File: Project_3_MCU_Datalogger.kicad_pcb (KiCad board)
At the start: 2 copper layers, 0 parts

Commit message: setup feuille PCB et importation 3D models
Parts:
- added BT1: Battery, Connector_PinHeader_2.54mm:PinHeader_1x02_P2.54mm_Vertical, F.Cu at (126.4, 94.8)
- added C1: 0.1u, Capacitor_SMD:C_0805_2012Metric, F.Cu at (148.8, 84.9)
- added C2: 0.1u, Capacitor_SMD:C_0805_2012Metric, F.Cu at (148.8, 87.9)
- added C3: 22p, Capacitor_SMD:C_0805_2012Metric, F.Cu at (148.8, 91.0)
- added C4: 22p, Capacitor_SMD:C_0805_2012Metric, F.Cu at (148.8, 94.0)
- added C5: 100n, Capacitor_SMD:C_0805_2012Metric, F.Cu at (148.8, 97.0)
- added D1: LED, LED_SMD:LED_0805_2012Metric, F.Cu at (153.2, 85.0)
- added D2: LED, LED_SMD:LED_0805_2012Metric, F.Cu at (153.2, 88.0)
- added H1: MountingHole, MountingHole:MountingHole_2.1mm, F.Cu at (127.0, 72.4)
- added H2: MountingHole, MountingHole:MountingHole_2.1mm, F.Cu at (127.0, 78.1)
- added H3: MountingHole, MountingHole:MountingHole_2.1mm, F.Cu at (127.0, 83.9)
- added H4: MountingHole, MountingHole:MountingHole_2.1mm, F.Cu at (127.0, 89.6)
- added J1: Conn_01x04_Pin, Connector_PinSocket_2.54mm:PinSocket_1x04_P2.54mm_Vertical, F.Cu at (164.3, 71.8)
- added J2: Conn_01x04_Pin, Connector_PinSocket_2.54mm:PinSocket_1x04_P2.54mm_Vertical, F.Cu at (168.9, 71.8)
- added J3: Conn_01x09_Pin, Connector_PinSocket_2.54mm:PinSocket_1x09_P2.54mm_Vertical, F.Cu at (159.7, 71.8)
- added J4: Conn_02x03_Odd_Even, Connector_PinSocket_2.54mm:PinSocket_2x03_P2.54mm_Vertical, F.Cu at (166.9, 84.0)
- added R1: 4.7k, Resistor_SMD:R_0805_2012Metric, F.Cu at (132.1, 71.0)
- added R2: 4.7k, Resistor_SMD:R_0805_2012Metric, F.Cu at (132.1, 73.9)
- added R3: 10k, Resistor_SMD:R_0805_2012Metric, F.Cu at (132.1, 76.9)
- added R4: 10k, Resistor_SMD:R_0805_2012Metric, F.Cu at (132.1, 79.8)
- added R5: 330, Resistor_SMD:R_0805_2012Metric, F.Cu at (132.1, 82.8)
- added R6: 10k, Resistor_SMD:R_0805_2012Metric, F.Cu at (132.1, 85.7)
- added R7: 330, Resistor_SMD:R_0805_2012Metric, F.Cu at (132.1, 88.7)
- added U1: 24LC1025, Package_SO:SOIC-8_5.3x5.3mm_P1.27mm, F.Cu at (139.5, 73.0)
- added U2: 24LC1025, Package_SO:SOIC-8_5.3x5.3mm_P1.27mm, F.Cu at (139.5, 80.0)
- added U3: DS1337S_, DS1337S_:SOIC127P600X175-8N, F.Cu at (139.5, 98.1)
- added U4: ATMEGA328P-AU, ATMEGA328P-AU:QFP80P900X900X120-32N, F.Cu at (140.9, 89.1)
- added Y1: 16MHz, Crystal:Crystal_SMD_5032-2Pin_5.0x3.2mm_HandSoldering, F.Cu at (149.8, 72.1)
- added Y2: 32.768 kHz, Crystal:Crystal_SMD_5032-2Pin_5.0x3.2mm_HandSoldering, F.Cu at (149.8, 77.4)

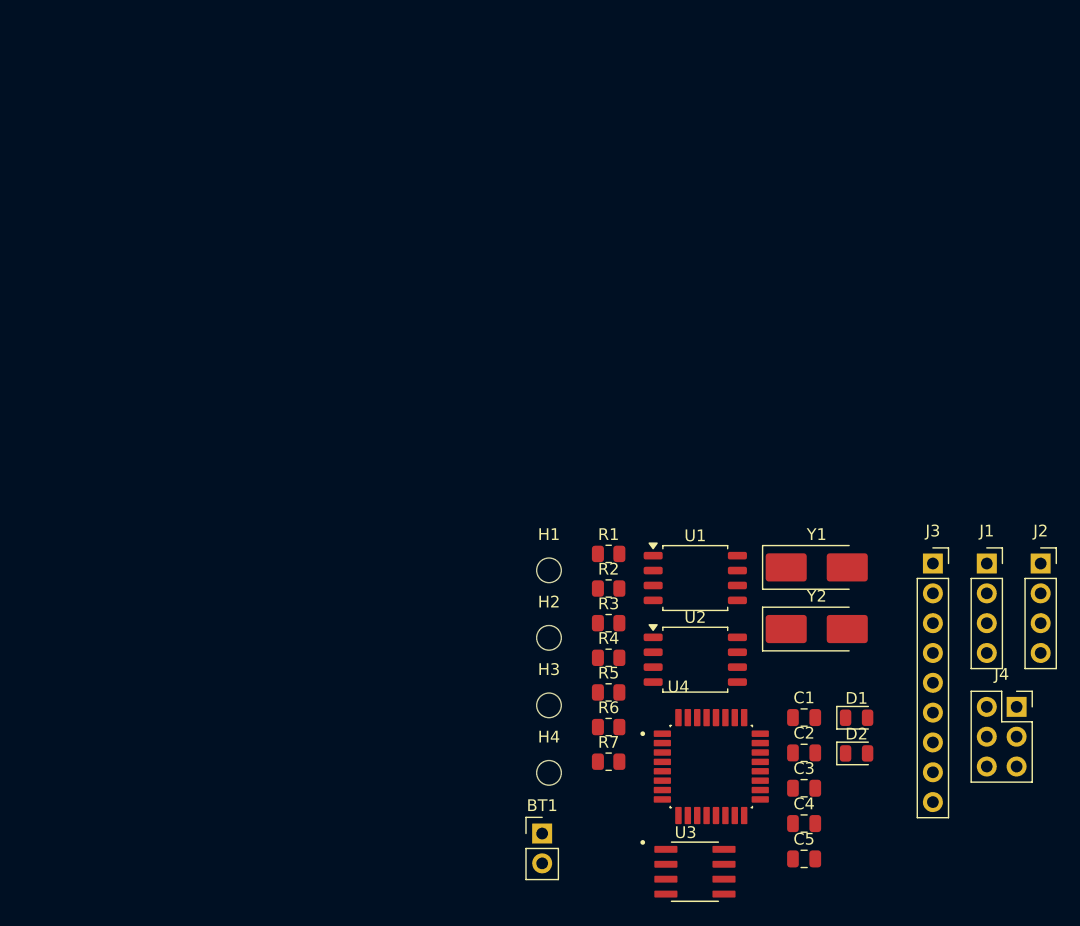
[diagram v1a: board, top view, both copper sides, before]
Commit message: Placement des composants avant routage
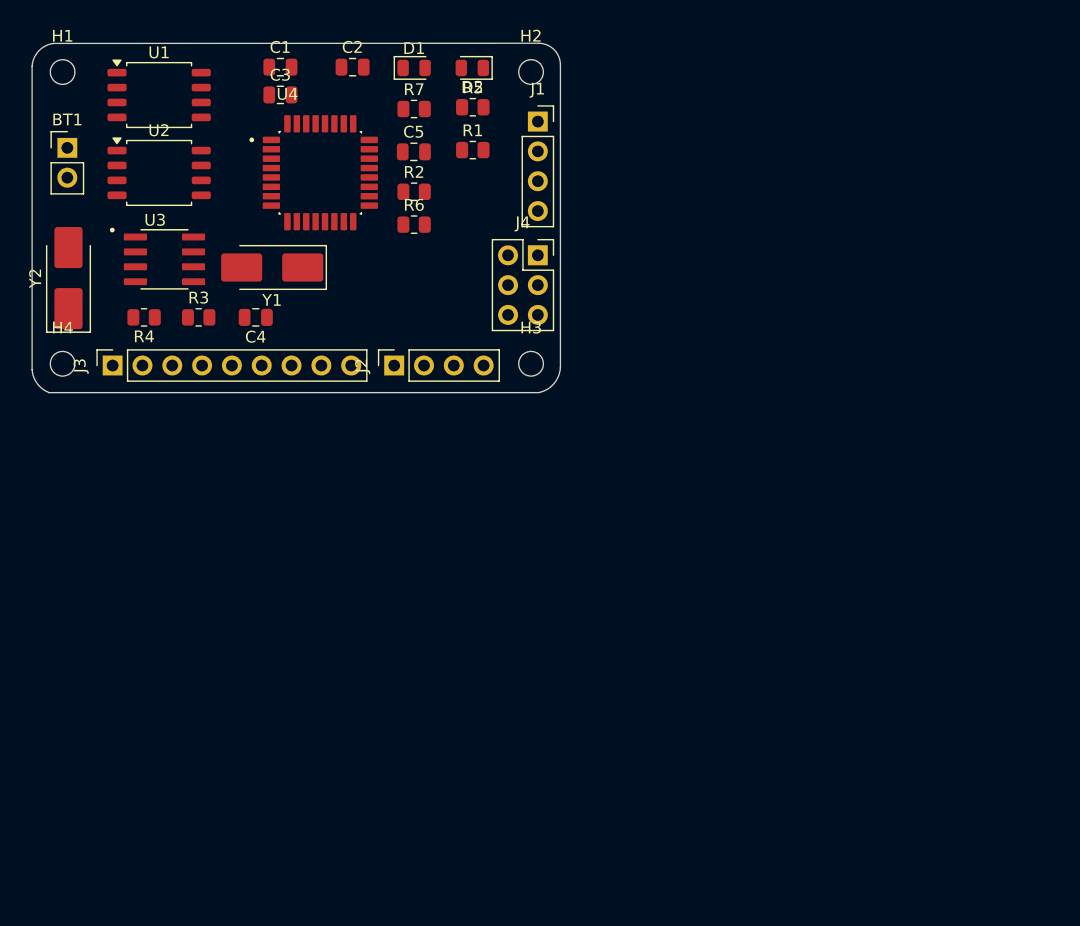
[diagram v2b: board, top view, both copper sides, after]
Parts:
- moved C3 74.0 mm to (104.2, 31.9)
- moved J3 71.9 mm to (89.9, 55.0), turned to 90 degrees
- moved C1 71.1 mm to (104.2, 29.5)
- moved BT1 71.0 mm to (86.0, 36.4)
- moved Y2 70.4 mm to (86.1, 47.5), turned to 90 degrees
- moved C2 69.9 mm to (110.3, 29.5)
- moved U3 69.0 mm to (94.3, 45.9)
- moved C5 68.8 mm to (115.5, 36.8)
- moved D1 67.0 mm to (115.5, 29.6)
- moved D2 66.9 mm to (120.5, 29.6), turned to 180 degrees
- moved C4 63.6 mm to (102.0, 50.9), turned to 180 degrees
- moved U2 61.7 mm to (93.8, 38.5)
- moved U1 61.5 mm to (93.8, 31.9)
- moved U4 60.6 mm to (107.5, 38.5)
- moved H1 59.3 mm to (85.6, 29.9)
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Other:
- board outline added: 45 x 29.8 mm

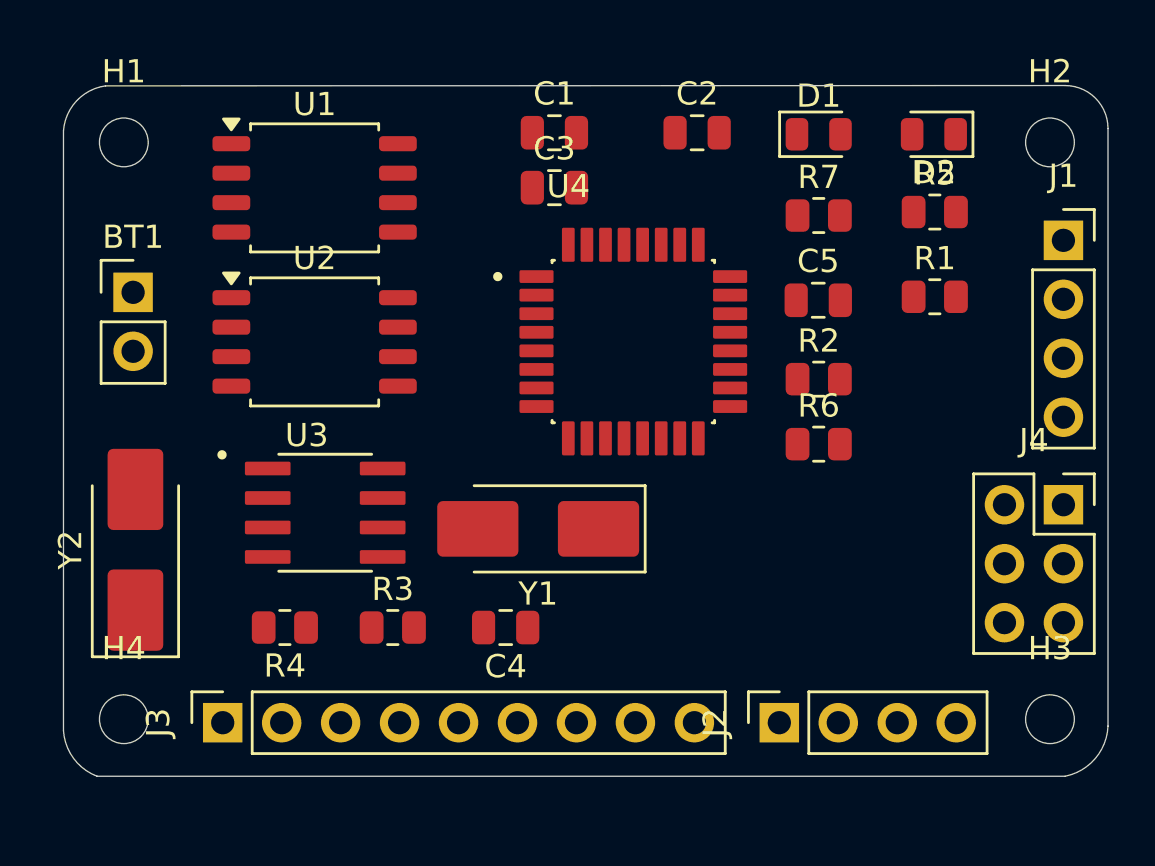
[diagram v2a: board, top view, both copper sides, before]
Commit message: amelioration disposition composants et changements circuit
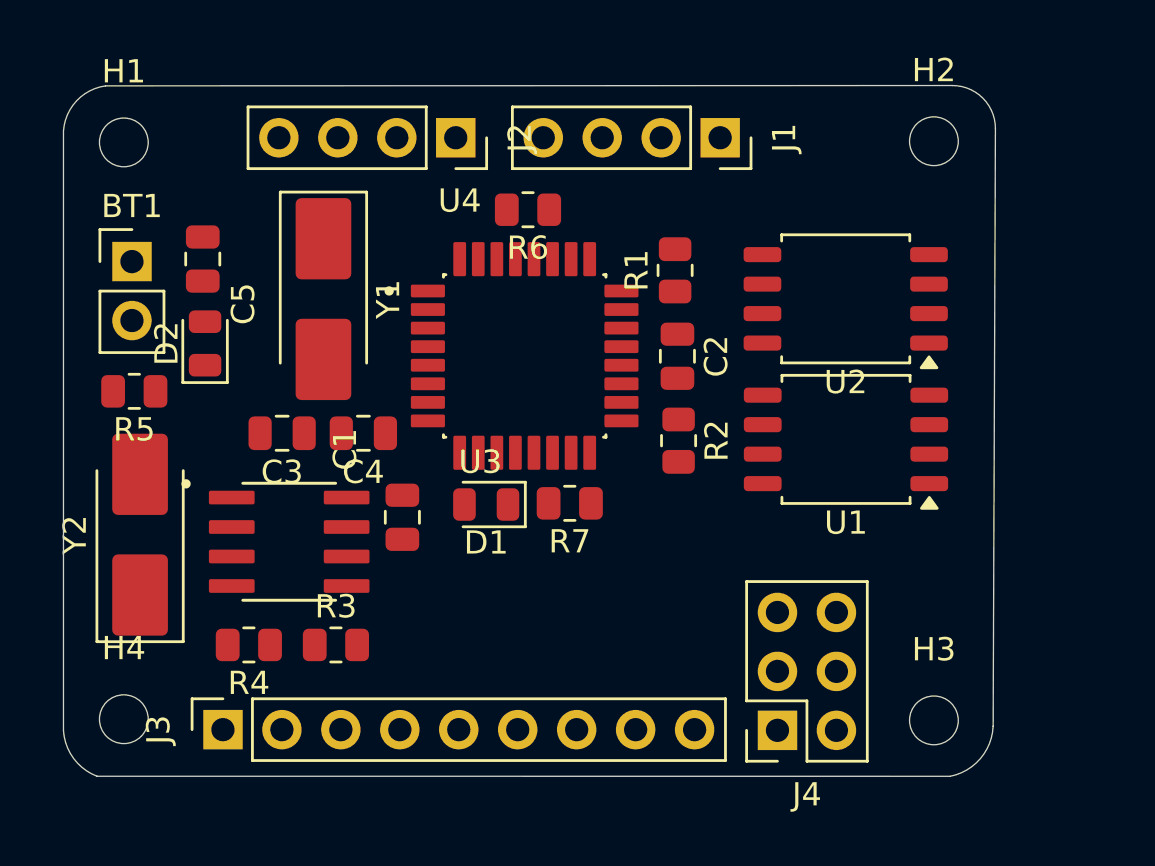
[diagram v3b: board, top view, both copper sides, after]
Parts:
- moved R5 35.3 mm to (86.0, 40.7), turned to 180 degrees
- moved D2 32.7 mm to (89.1, 38.6), turned to 90 degrees
- moved J2 28.8 mm to (99.9, 29.8), turned to -90 degrees
- moved C5 26.6 mm to (89.0, 35.0), turned to -90 degrees
- moved U1 25.3 mm to (116.7, 42.7), turned to 180 degrees
- moved U2 23.0 mm to (116.7, 36.7), turned to 180 degrees
- moved D1 21.4 mm to (101.2, 45.5), turned to 180 degrees
- moved C1 17.8 mm to (97.6, 46.1), turned to 90 degrees
- moved R7 16.4 mm to (104.8, 45.5), turned to 180 degrees
- moved R6 16.1 mm to (103.0, 32.9), turned to 180 degrees
- moved C3 15.8 mm to (92.4, 42.5), turned to 180 degrees
- moved J4 15.7 mm to (113.8, 55.3), turned to 180 degrees
- moved J1 15.4 mm to (111.3, 29.8), turned to -90 degrees
- moved Y1 13.5 mm to (94.2, 36.7), turned to -90 degrees
- moved R1 11.2 mm to (109.3, 35.5), turned to 90 degrees
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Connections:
- BT1 pad 1: Net-(BT1-+) -> /Vcc
- C5 pad 1: Net-(BT1-+) -> /Vcc
- D1 pad 2: /SCL -> Net-(D1-A)
- D2 pad 2: Net-(BT1-+) -> /Vcc
- U4 pad 13: unconnected-(U4-PB1-Pad13) -> Net-(D1-A)
- U4 pad 17: /SCL -> /SCK
- U4 pad 18: Net-(BT1-+) -> /Vcc
- U4 pad 4: Net-(BT1-+) -> /Vcc
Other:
- board size 45 x 29.8 mm -> 40.2 x 29.8 mm

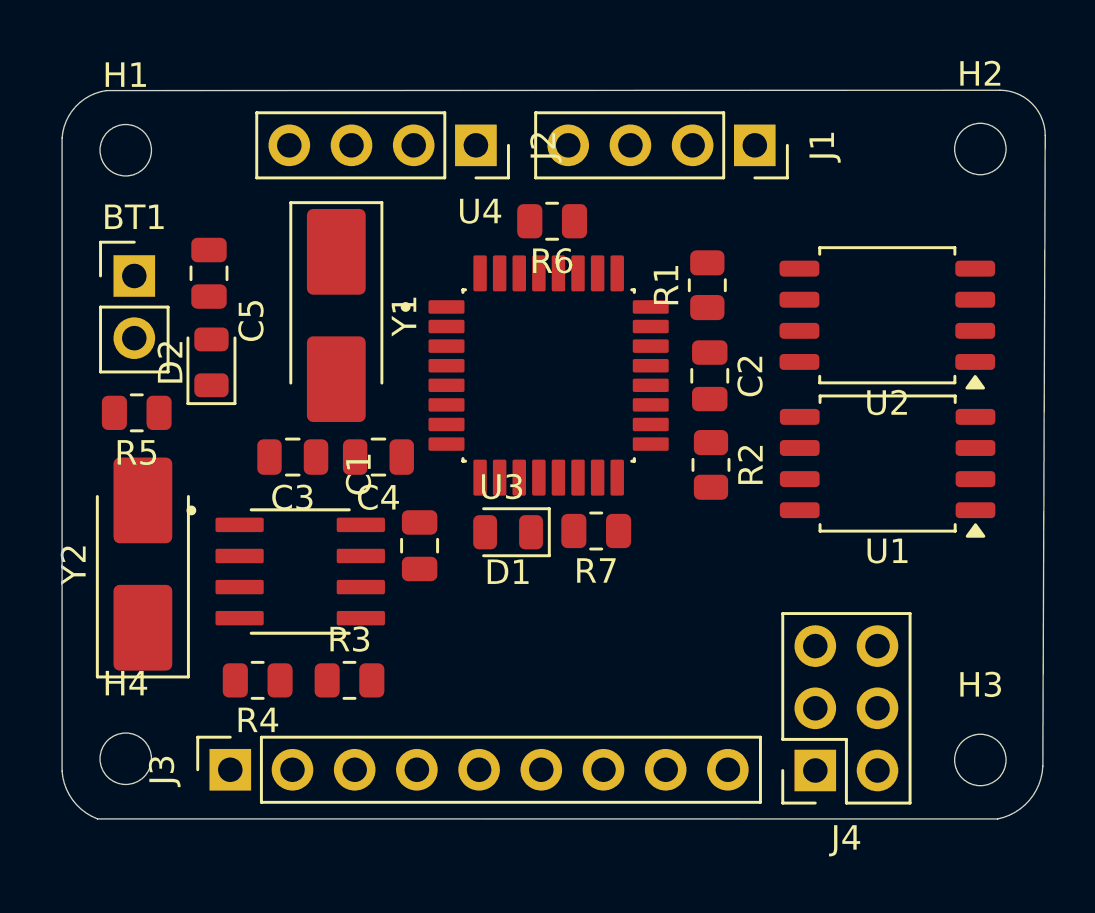
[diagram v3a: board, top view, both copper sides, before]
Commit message: Fin du routage sur deux couches et modifications du schema
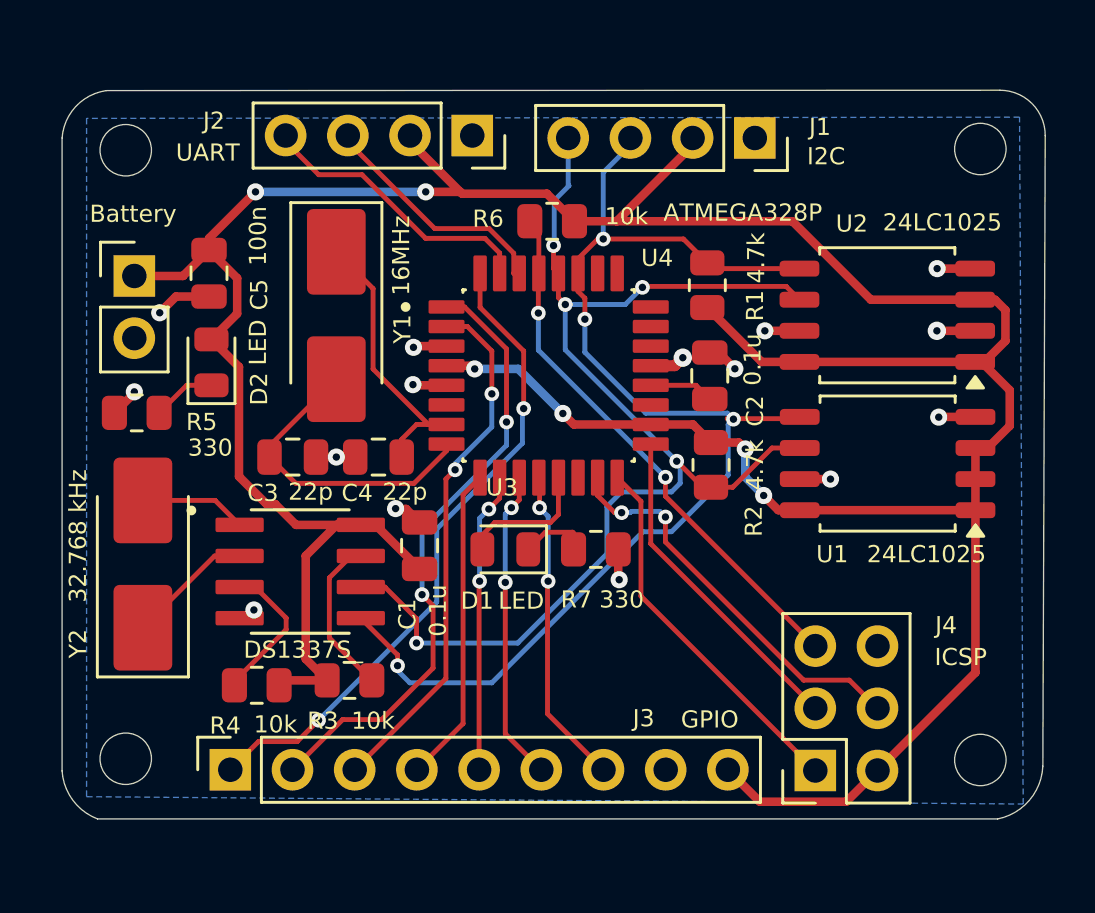
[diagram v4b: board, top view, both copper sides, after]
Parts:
- added REF**: KiCad-Logo2_5mm_SilkScreen, Symbol:KiCad-Logo2_5mm_SilkScreen, B.Cu at (102.8, 47.8)
- U4: value ATMEGA328P-AU -> ATMEGA328P
- moved R7 0.75 mm to (104.8, 46.2)
- moved D1 0.71 mm to (101.1, 46.2)
- moved J2 0.43 mm to (99.8, 29.4)
- moved J1 0.30 mm to (111.3, 29.4)
- moved R4 0.20 mm to (91.0, 51.8)
- renumbered BT1 to Battery
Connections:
- J4 pad 3: /SCL -> /SCK
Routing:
- net /Vcc: track 0.00 -> 143.9 mm, vias 0 -> 6
- net /SCL: track 0.00 -> 51.6 mm, vias 0 -> 5
- net /SDA: track 0.00 -> 51.0 mm, vias 0 -> 4
- net /D2: track 0.00 -> 26.9 mm, vias 0 -> 2
- net /D3: track 0.00 -> 25.3 mm, vias 0 -> 2
- net /RESET: track 0.00 -> 22.2 mm, vias 0 -> 2
- net /D4: track 0.00 -> 21.7 mm, vias 0 -> 2
- net GND: track 0.00 -> 21.7 mm, vias 0 -> 15
- net /MOSI: track 0.00 -> 16.4 mm, vias 0 -> 2
- net /MISO: track 0.00 -> 15.3 mm
- net /SCK: track 0.00 -> 13.6 mm
- net Net-(U4-PB7): track 0.00 -> 13.4 mm
- net /D8: track 0.00 -> 13.0 mm, vias 0 -> 2
- net /D5: track 0.00 -> 13.0 mm
- net /D7: track 0.00 -> 12.8 mm, vias 0 -> 2
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- added copper zone on B.Cu, net GND
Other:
- board text added: "Author : Guillaume LOUIS"
- board text added: "Project MCU datalogger"
- board text added: "Version 1.0, 2 layers"
